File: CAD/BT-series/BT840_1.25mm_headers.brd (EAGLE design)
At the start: 33.4 x 25.1 mm, 64 parts, among them J1 SM02B-SRSS-TB(LF)(SN), U1 TPD4S012DRYR, U2 BT840, U3 LP5907MFX-3.3/NOPB, U4 LP5907MFX-3.3/NOPB, U5 ADS131M08IPBS, U6 BQ24072RGTR, U7 DX4R005JJ2R1800, X1 ABM3B-8.000MHZ-B2-T, X2 FC-12M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

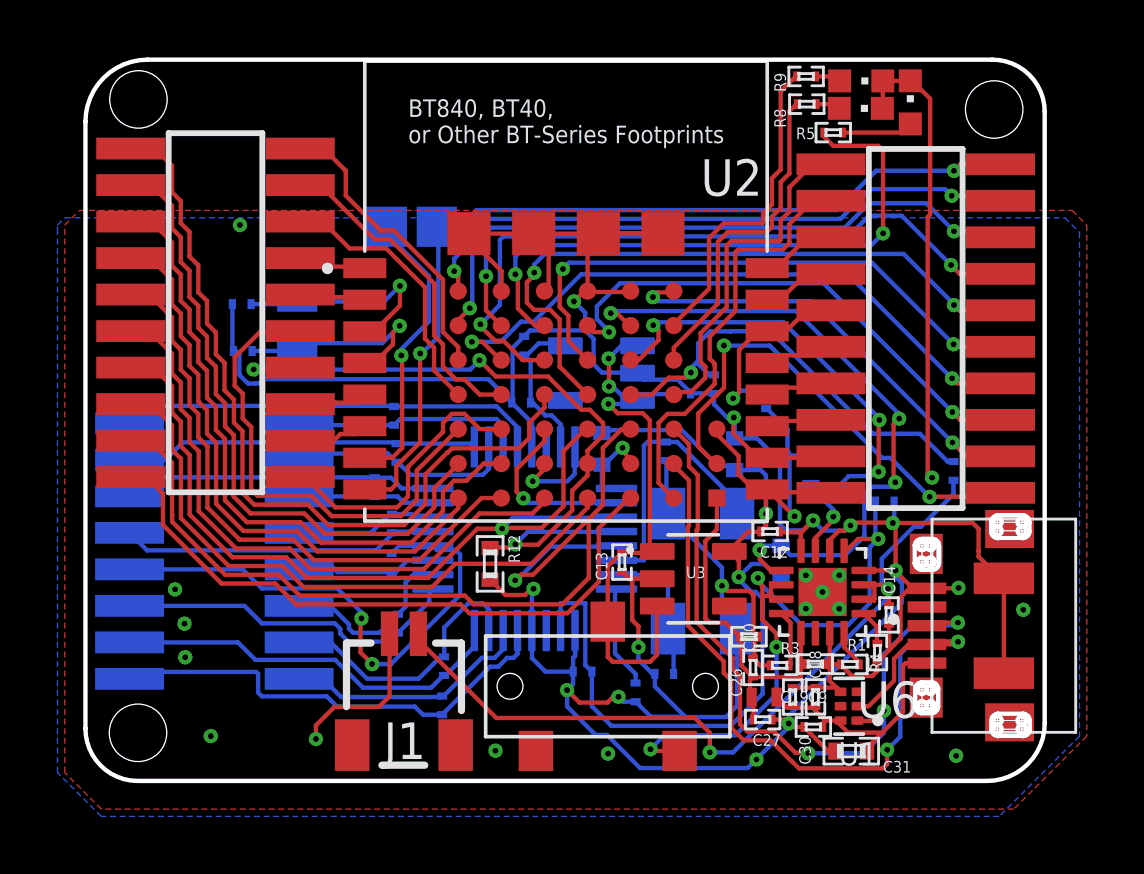
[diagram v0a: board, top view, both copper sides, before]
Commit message: Update BT840_1.25mm_headers.brd
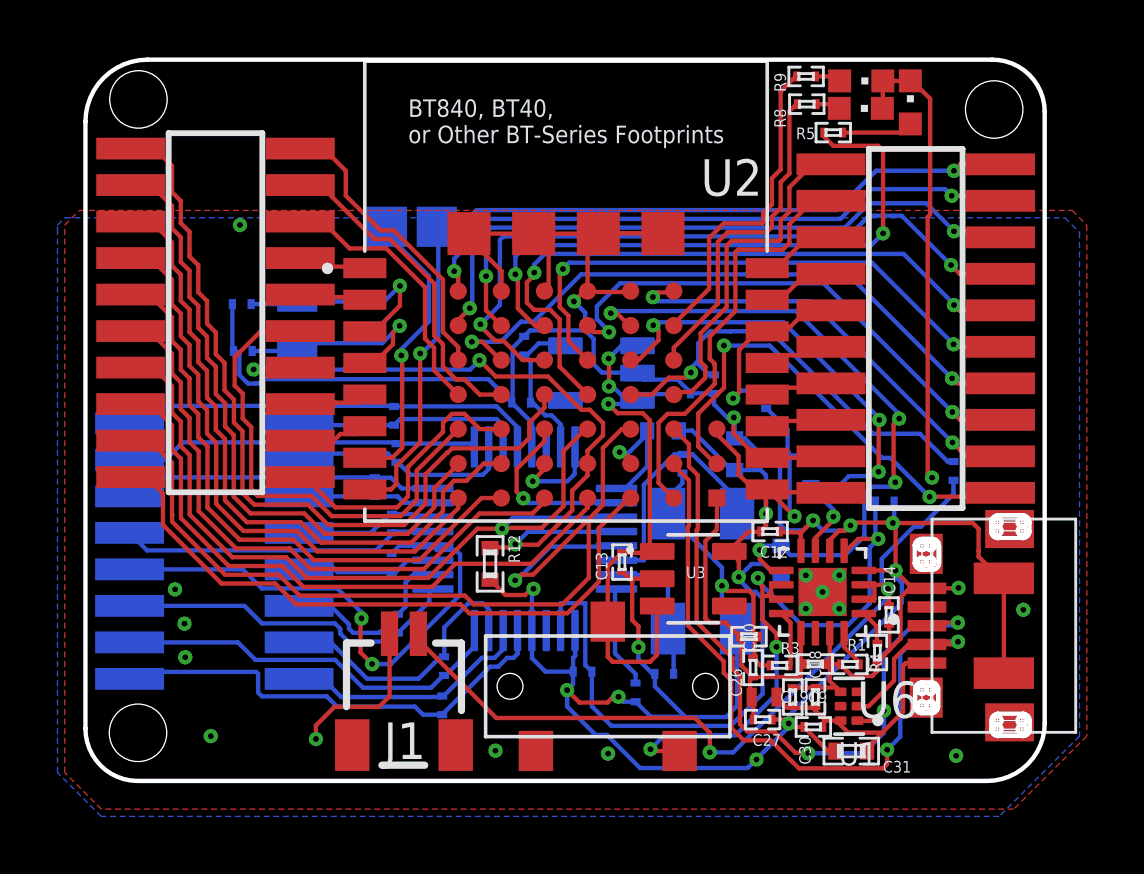
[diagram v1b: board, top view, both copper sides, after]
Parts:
- moved R13 2.22 mm to (27.4, 54.1), turned to 180 degrees
- moved C4 0.72 mm to (28.1, 52.9)
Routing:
- net VDD: track 42.8 -> 40.2 mm
- net CS: track 2.93 -> 4.68 mm
- net CLKOUT: track 9.51 -> 8.41 mm
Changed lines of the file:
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@@
 <attribute name="VALUE" x="28.095196875" y="44.709078125" size="0.4064" layer="28" font="vector" rot="MR0"/>
 </element>
-<element name="C4" library="standardparts" package="0201" value="10pF" x="27.522425" y="53.34305" smashed="yes" rot="MR270">
-<attribute name="NAME" x="27.014425" y="53.97805" size="0.4064" layer="26" font="vector" rot="MR270"/>
-<attribute name="VALUE" x="28.411425" y="53.97805" size="0.4064" layer="28" font="vector" rot="MR270"/>
+<element name="C4" library="standardparts" package="0201" value="10pF" x="28.09189375" y="52.909725" smashed="yes" rot="MR270">
+<attribute name="NAME" x="27.58389375" y="53.544725" size="0.4064" layer="26" font="vector" rot="MR270"/>
+<attribute name="VALUE" x="28.98089375" y="53.544725" size="0.4064" layer="28" font="vector" rot="MR270"/>
 </element>
 <element name="U7" library="DX4R005JJ2R1800" package="DX4R005JJ2R1800" value="DX4R005JJ2R1800" x="38.12666875" y="47.274990625" smashed="yes" rot="R180">
@@
 <attribute name="VALUE" x="20.385534375" y="50.4421125" size="0.4064" layer="27" font="vector" rot="R270"/>
 </element>
-<element name="R13" library="standardparts" package="0402" value="100kΩ" x="25.289271875" y="53.428640625" smashed="yes" rot="MR90">
-<attribute name="NAME" x="25.804128125" y="54.580528125" size="0.4064" layer="26" font="vector" rot="MR0"/>
-<attribute name="VALUE" x="24.273271875" y="52.412640625" size="0.4064" layer="28" font="vector" rot="MR90"/>
+<element name="R13" library="standardparts" package="0402" value="100kΩ" x="27.418534375" y="54.053721875" smashed="yes" rot="MR180">
+<attribute name="NAME" x="28.570421875" y="53.538865625" size="0.4064" layer="26" font="vector" rot="MR90"/>
+<attribute name="VALUE" x="26.402534375" y="55.069721875" size="0.4064" layer="28" font="vector" rot="MR180"/>
 </element>
 <element name="U1" library="TPD4S012DRYR" package="PSON50P145X100X60-6N" value="TPD4S012DRYR" x="33.89198125" y="44.473875" smashed="yes" rot="R180">
@@
 <wire x1="29.88349375" y1="54.518559375" x2="29.8677" y2="54.502765625" width="0.1524" layer="1"/>
 <wire x1="29.8677" y1="54.502765625" x2="29.8677" y2="53.9675375" width="0.1524" layer="1"/>
-<wire x1="27.537540625" y1="51.228509375" x2="27.5374625" y2="53.0330875" width="0.1524" layer="16"/>
-<wire x1="27.522425" y1="53.01805" x2="27.5374625" y2="53.0330875" width="0.1524" layer="16"/>
+<wire x1="27.537540625" y1="51.228509375" x2="27.537521875" y2="51.677290625" width="0.1524" layer="16"/>
+<wire x1="28.09189375" y1="52.584725" x2="28.09189375" y2="52.2316625" width="0.1524" layer="16"/>
+<wire x1="28.09189375" y1="52.2316625" x2="27.537521875" y2="51.677290625" width="0.1524" layer="16"/>
 <wire x1="27.592928125" y1="51.17313125" x2="27.537540625" y2="51.228509375" width="0.1524" layer="16"/>
 <wire x1="30.718415625" y1="53.116821875" x2="29.8677" y2="53.9675375" width="0.1524" layer="1"/>
@@
 <wire x1="32.72281875" y1="45.123234375" x2="32.7177375" y2="45.118153125" width="0.1524" layer="1"/>
 <wire x1="32.7177375" y1="45.118153125" x2="31.93288125" y2="45.118153125" width="0.1524" layer="1"/>
-<wire x1="31.09963125" y1="53.19521875" x2="31.09963125" y2="53.381959375" width="0.1524" layer="16"/>
-<wire x1="31.09963125" y1="53.381959375" x2="30.691165625" y2="53.790425" width="0.1524" layer="16"/>
-<wire x1="29.9107875" y1="53.790425" x2="30.691165625" y2="53.790425" width="0.1524" layer="16"/>
+<wire x1="31.09963125" y1="53.19521875" x2="30.8619375" y2="53.19521875" width="0.1524" layer="16"/>
+<wire x1="30.8619375" y1="53.19521875" x2="30.26673125" y2="53.790425" width="0.1524" layer="16"/>
+<wire x1="29.9107875" y1="53.790425" x2="30.26673125" y2="53.790425" width="0.1524" layer="16"/>
 <wire x1="30.552134375" y1="46.14634375" x2="30.602384375" y2="46.19659375" width="0.1524" layer="1"/>
 <wire x1="31.151696875" y1="45.895259375" x2="30.80321875" y2="45.895259375" width="0.1524" layer="1"/>
@@
 <wire x1="30.054765625" y1="48.967925" x2="30.054765625" y2="48.857409375" width="0.1524" layer="16"/>
 <via x="31.00019375" y="51.17135" extent="1-16" drill="0.2"/>
-<wire x1="25.289271875" y1="53.978640625" x2="25.66271875" y2="54.08065625" width="0.1524" layer="16"/>
+<wire x1="28.432396875" y1="54.06756875" x2="27.97404375" y2="54.05923125" width="0.1524" layer="16"/>
+<wire x1="27.968534375" y1="54.053721875" x2="27.97404375" y2="54.05923125" width="0.1524" layer="16"/>
 <wire x1="29.9107875" y1="52.690425" x2="29.771421875" y2="52.829790625" width="0.1524" layer="16"/>
-<wire x1="29.32295625" y1="52.829790625" x2="29.771421875" y2="52.829790625" width="0.1524" layer="16"/>
+<wire x1="29.670175" y1="52.829790625" x2="29.771421875" y2="52.829790625" width="0.1524" layer="16"/>
 <wire x1="31.00019375" y1="51.17135" x2="31.00019375" y2="52.510465625" width="0.1524" layer="16"/>
 <wire x1="31.00019375" y1="52.510465625" x2="30.82020625" y2="52.690425" width="0.1524" layer="16"/>
@@
 <wire x1="31.00019375" y1="50.73308125" x2="30.820225" y2="50.5531125" width="0.1524" layer="1"/>
 <wire x1="30.883859375" y1="48.215003125" x2="30.883859375" y2="44.90470625" width="0.1524" layer="16"/>
-<wire x1="25.66271875" y1="54.08065625" x2="28.072090625" y2="54.08065625" width="0.1524" layer="16"/>
-<wire x1="28.072090625" y1="54.08065625" x2="29.32295625" y2="52.829790625" width="0.1524" layer="16"/>
+<wire x1="28.432396875" y1="54.06756875" x2="29.670175" y2="52.829790625" width="0.1524" layer="16"/>
 <wire x1="25.62186875" y1="43.7903625" x2="29.769515625" y2="43.7903625" width="0.1524" layer="16"/>
 <wire x1="29.769515625" y1="43.7903625" x2="30.883859375" y2="44.90470625" width="0.1524" layer="16"/>
@@
 <contactref element="U2" pad="D5"/>
 <wire x1="26.293384375" y1="52.916821875" x2="26.293384375" y2="53.06315625" width="0.1524" layer="1"/>
-<wire x1="26.293384375" y1="53.06315625" x2="26.01146875" y2="53.345071875" width="0.1524" layer="1"/>
-<wire x1="26.01146875" y1="53.345071875" x2="26.01146875" y2="53.4619125" width="0.1524" layer="1"/>
-<via x="26.01146875" y="53.4619125" extent="1-16" drill="0.2"/>
-<wire x1="26.01146875" y1="53.4619125" x2="25.909615625" y2="53.360059375" width="0.1524" layer="16"/>
-<wire x1="25.909615625" y1="53.360059375" x2="25.8585625" y2="53.360059375" width="0.1524" layer="16"/>
-<wire x1="25.8585625" y1="53.360059375" x2="25.37714375" y2="52.878640625" width="0.1524" layer="16"/>
-<wire x1="25.289271875" y1="52.878640625" x2="25.37714375" y2="52.878640625" width="0.1524" layer="16"/>
-<wire x1="25.289271875" y1="52.112221875" x2="25.289271875" y2="52.878640625" width="0.1524" layer="16"/>
-<wire x1="25.801" y1="52.051653125" x2="25.349840625" y2="52.051653125" width="0.1524" layer="16"/>
-<wire x1="25.349840625" y1="52.051653125" x2="25.289271875" y2="52.112221875" width="0.1524" layer="16"/>
+<wire x1="26.293384375" y1="53.06315625" x2="25.975146875" y2="53.381396875" width="0.1524" layer="1"/>
+<wire x1="25.975146875" y1="53.381396875" x2="25.90681875" y2="53.31306875" width="0.1524" layer="1"/>
+<via x="25.90681875" y="53.31306875" extent="1-16" drill="0.2"/>
+<wire x1="26.868534375" y1="54.053721875" x2="26.868534375" y2="53.94094375" width="0.1524" layer="16"/>
+<wire x1="26.868534375" y1="54.053721875" x2="26.868534375" y2="52.814134375" width="0.1524" layer="16"/>
+<wire x1="26.868534375" y1="52.814134375" x2="26.106053125" y2="52.051653125" width="0.1524" layer="16"/>
+<wire x1="25.801" y1="52.051653125" x2="26.106053125" y2="52.051653125" width="0.1524" layer="16"/>
+<wire x1="26.868534375" y1="53.94094375" x2="26.211196875" y2="53.28360625" width="0.1524" layer="16"/>
+<wire x1="26.211196875" y1="53.28360625" x2="25.93628125" y2="53.28360625" width="0.1524" layer="16"/>
+<wire x1="25.90681875" y1="53.31306875" x2="25.93628125" y2="53.28360625" width="0.1524" layer="16"/>
 </signal>
 <signal name="DRDY">
@@
 <contactref element="X1" pad="3"/>
 <contactref element="C4" pad="1"/>
-<wire x1="29.992928125" y1="51.17313125" x2="29.992928125" y2="51.58523125" width="0.1524" layer="16"/>
-<wire x1="29.992928125" y1="51.58523125" x2="27.910109375" y2="53.66805" width="0.1524" layer="16"/>
+<wire x1="29.992928125" y1="51.17313125" x2="29.992928125" y2="51.69013125" width="0.1524" layer="16"/>
+<wire x1="29.992928125" y1="51.69013125" x2="28.448334375" y2="53.234725" width="0.1524" layer="16"/>
 <wire x1="26.74934375" y1="49.551653125" x2="25.801" y2="49.551653125" width="0.1524" layer="16"/>
-<wire x1="26.74934375" y1="49.551653125" x2="26.74934375" y2="53.53753125" width="0.1524" layer="16"/>
-<wire x1="27.522425" y1="53.66805" x2="27.910109375" y2="53.66805" width="0.1524" layer="16"/>
-<wire x1="27.522425" y1="53.66805" x2="27.51734375" y2="53.67313125" width="0.1524" layer="16"/>
-<wire x1="27.51734375" y1="53.67313125" x2="26.88494375" y2="53.67313125" width="0.1524" layer="16"/>
-<wire x1="26.88494375" y1="53.67313125" x2="26.74934375" y2="53.53753125" width="0.1524" layer="16"/>
+<wire x1="26.74934375" y1="49.551653125" x2="26.74934375" y2="52.176346875" width="0.1524" layer="16"/>
+<wire x1="28.09189375" y1="53.234725" x2="28.448334375" y2="53.234725" width="0.1524" layer="16"/>
+<wire x1="28.09189375" y1="53.234725" x2="27.807721875" y2="53.234725" width="0.1524" layer="16"/>
+<wire x1="27.807721875" y1="53.234725" x2="26.74934375" y2="52.176346875" width="0.1524" layer="16"/>
 </signal>
 <signal name="TMR">

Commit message: -
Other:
- board text removed: "TOP"
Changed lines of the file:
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@@
 <grid distance="0.01" unitdist="mil" unit="mil" style="lines" multiple="1" display="no" altdistance="5" altunitdist="mil" altunit="mil"/>
 <layers>
-<layer number="1" name="Top" color="4" fill="1" visible="yes" active="yes"/>
+<layer number="1" name="Top" color="4" fill="1" visible="no" active="yes"/>
 <layer number="2" name="Route2" color="16" fill="1" visible="no" active="no"/>
 <layer number="3" name="Route3" color="17" fill="1" visible="no" active="no"/>
@@
 <layer number="19" name="Unrouted" color="6" fill="1" visible="yes" active="yes"/>
 <layer number="20" name="Dimension" color="24" fill="1" visible="yes" active="yes"/>
-<layer number="21" name="tPlace" color="7" fill="1" visible="yes" active="yes"/>
+<layer number="21" name="tPlace" color="7" fill="1" visible="no" active="yes"/>
 <layer number="22" name="bPlace" color="7" fill="1" visible="yes" active="yes"/>
-<layer number="23" name="tOrigins" color="15" fill="1" visible="yes" active="yes"/>
+<layer number="23" name="tOrigins" color="15" fill="1" visible="no" active="yes"/>
 <layer number="24" name="bOrigins" color="15" fill="1" visible="yes" active="yes"/>
-<layer number="25" name="tNames" color="7" fill="1" visible="yes" active="yes"/>
+<layer number="25" name="tNames" color="7" fill="1" visible="no" active="yes"/>
 <layer number="26" name="bNames" color="7" fill="1" visible="yes" active="yes"/>
 <layer number="27" name="tValues" color="7" fill="1" visible="no" active="yes"/>
@@
 <layer number="37" name="tTest" color="7" fill="1" visible="no" active="yes"/>
 <layer number="38" name="bTest" color="7" fill="1" visible="no" active="yes"/>
-<layer number="39" name="tKeepout" color="4" fill="11" visible="yes" active="yes"/>
+<layer number="39" name="tKeepout" color="4" fill="11" visible="no" active="yes"/>
 <layer number="40" name="bKeepout" color="1" fill="11" visible="yes" active="yes"/>
-<layer number="41" name="tRestrict" color="4" fill="10" visible="yes" active="yes"/>
+<layer number="41" name="tRestrict" color="4" fill="10" visible="no" active="yes"/>
 <layer number="42" name="bRestrict" color="1" fill="10" visible="yes" active="yes"/>
 <layer number="43" name="vRestrict" color="2" fill="10" visible="no" active="yes"/>
@@
 <layer number="49" name="Reference" color="7" fill="1" visible="no" active="yes"/>
 <layer number="50" name="dxf" color="7" fill="1" visible="no" active="yes"/>
-<layer number="51" name="tDocu" color="7" fill="1" visible="yes" active="yes"/>
+<layer number="51" name="tDocu" color="7" fill="1" visible="no" active="yes"/>
 <layer number="52" name="bDocu" color="7" fill="1" visible="yes" active="yes"/>
 <layer number="53" name="tGND_GNDA" color="7" fill="9" visible="no" active="no"/>
@@
    BOJAN JOVANOVICH
      AGPL v3 LICENSE</text>
-<text x="25.880315625" y="58.8586625" size="0.3048" layer="22" rot="MR0">TOP</text>
 <hole x="9.16685625" y="65.585340625" drill="2"/>
 <hole x="38.940740625" y="65.234821875" drill="2"/>
@@
 <attribute name="MF" value="Texas Instruments" x="-25.17419375" y="63.21298125" size="1.778" layer="28" rot="MR180" display="off"/>
 <attribute name="MP" value="ADS131M08IPBS" x="-25.17419375" y="63.21298125" size="1.778" layer="28" rot="MR180" display="off"/>
-<attribute name="NAME" x="22.193509375" y="51.23574375" size="1.27" layer="26" rot="MR0"/>
+<attribute name="NAME" x="22.50846875" y="51.180115625" size="1.27" layer="26" rot="MR0"/>
 <attribute name="PACKAGE" value="TQFP-32 Texas Instruments" x="-25.17419375" y="63.21298125" size="1.778" layer="28" rot="MR180" display="off"/>
 <attribute name="PRICE" value="None" x="-25.17419375" y="63.21298125" size="1.778" layer="28" rot="MR180" display="off"/>
@@
 </element>
 <element name="R2" library="standardparts" package="0201" value="100kΩ" x="31.005271875" y="55.15483125" smashed="yes" rot="MR270">
-<attribute name="NAME" x="30.497271875" y="55.78983125" size="0.4064" layer="26" font="vector" rot="MR270"/>
+<attribute name="NAME" x="31.99409375" y="55.380634375" size="0.4064" layer="26" font="vector" rot="MR270"/>
 <attribute name="VALUE" x="31.894271875" y="55.78983125" size="0.4064" layer="28" font="vector" rot="MR270"/>
 </element>
@@
 <wire x1="26.4206625" y1="55.311040625" x2="27.025603125" y2="55.311040625" width="0.1524" layer="1"/>
 <wire x1="27.6199625" y1="55.9054" x2="27.025603125" y2="55.311040625" width="0.1524" layer="1"/>
-<wire x1="31.157475" y1="57.51974375" x2="29.77641875" y2="57.51974375" width="0.1524" layer="16"/>
+<wire x1="31.16445" y1="57.51276875" x2="29.052925" y2="57.51276875" width="0.1524" layer="16"/>
 <wire x1="37.525196875" y1="52.9844" x2="37.525196875" y2="52.986825" width="0.1524" layer="16"/>
-<wire x1="29.77641875" y1="57.51974375" x2="29.76944375" y2="57.51276875" width="0.1524" layer="16"/>
-<wire x1="29.76944375" y1="57.51276875" x2="29.052925" y2="57.51276875" width="0.1524" layer="16"/>
 <wire x1="29.052925" y1="57.51276875" x2="28.64269375" y2="57.1025375" width="0.1524" layer="16"/>
 <wire x1="28.64269375" y1="56.4929375" x2="28.232959375" y2="56.083203125" width="0.1524" layer="16"/>
@@
 <wire x1="28.64269375" y1="56.4929375" x2="28.64269375" y2="56.38139375" width="0.1524" layer="16"/>
 <wire x1="28.38869375" y1="56.083203125" x2="28.232959375" y2="56.083203125" width="0.1524" layer="16"/>
-<wire x1="31.157475" y1="57.51974375" x2="34.72489375" y2="53.952325" width="0.1524" layer="16"/>
+<wire x1="31.16445" y1="57.51276875" x2="34.72489375" y2="53.952325" width="0.1524" layer="16"/>
 <wire x1="37.525196875" y1="52.986825" x2="37.321996875" y2="52.986825" width="0.1524" layer="16"/>
 <wire x1="37.321996875" y1="52.986825" x2="36.3564875" y2="53.952334375" width="0.1524" layer="16"/>
